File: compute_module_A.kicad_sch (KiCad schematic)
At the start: 14 parts, among them J12 MagJack, J13 Micro_SD_Card_Det, U1 RT9742GGJ5

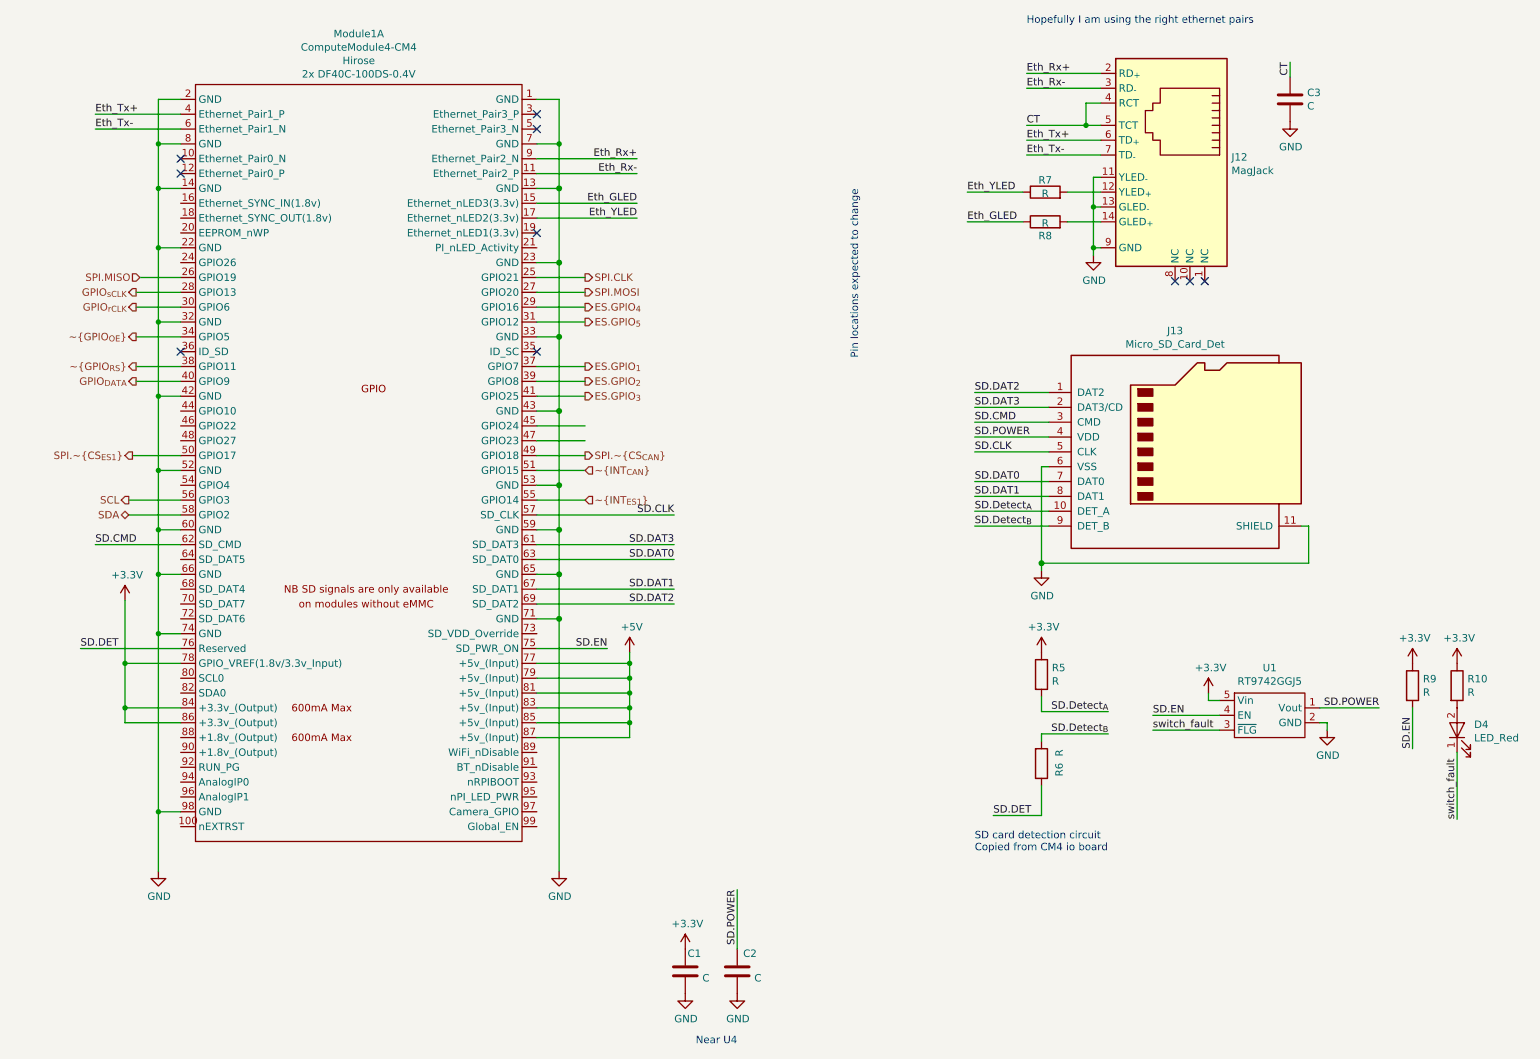
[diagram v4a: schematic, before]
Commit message: Cleaning up
Reassigned reference designators to better match their position on the board.
Moved USB hub IC and related circuits to their own sheet in the schematic.
Tweaked reference designator positions on board to improve visibility.
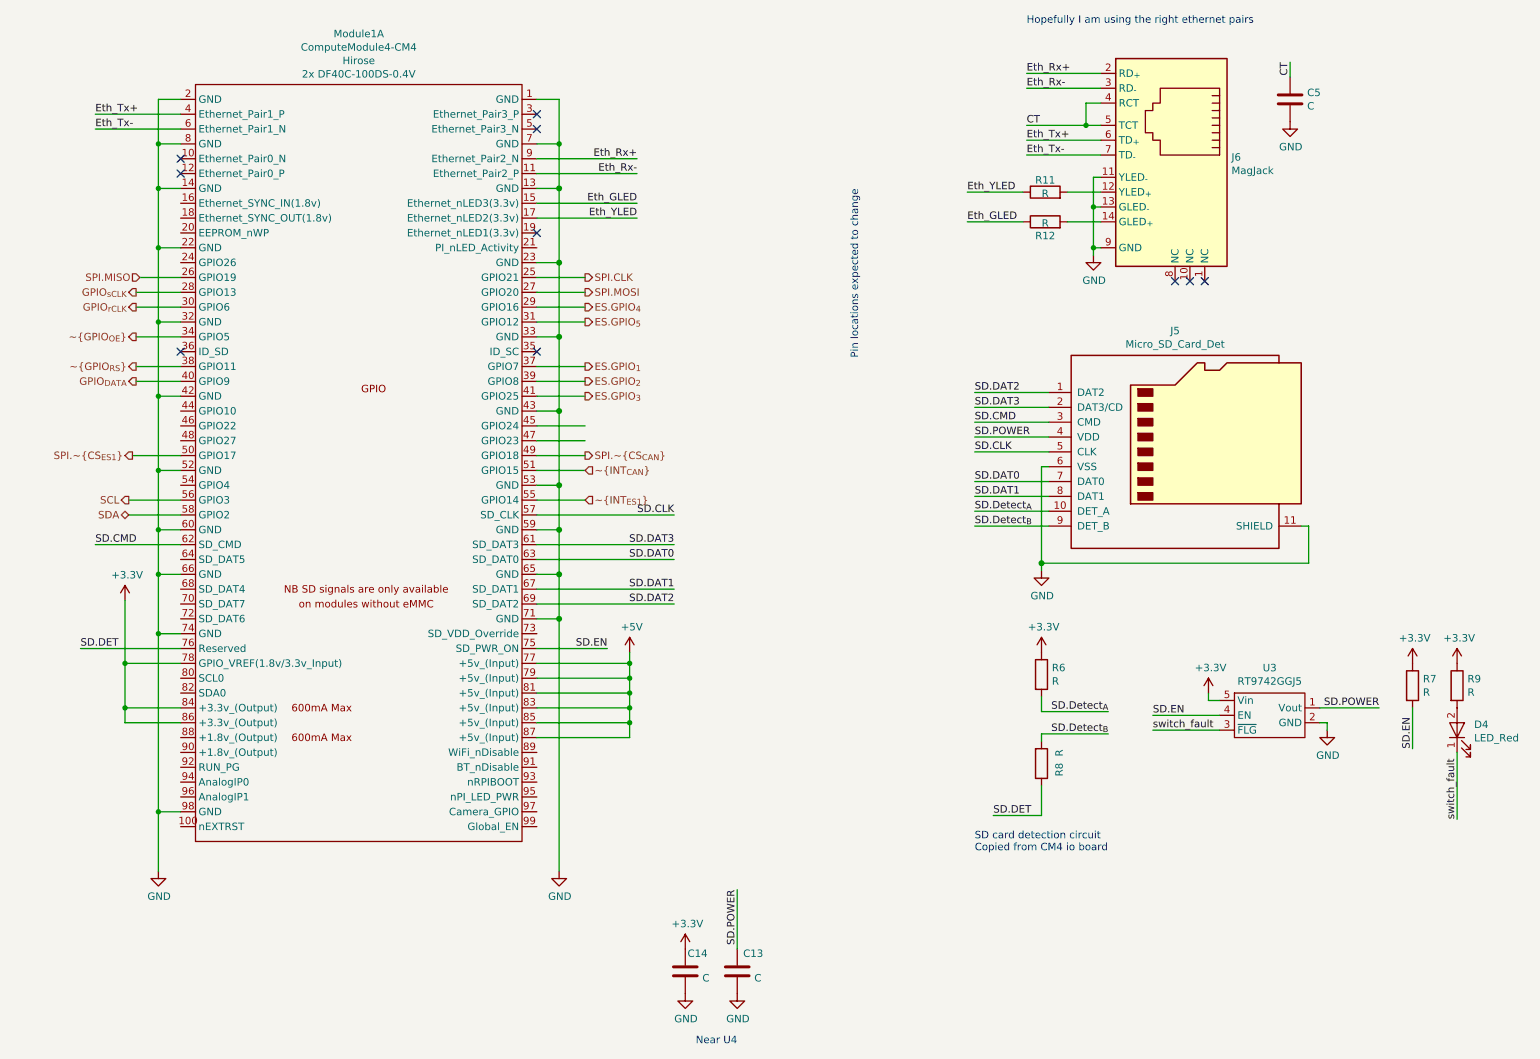
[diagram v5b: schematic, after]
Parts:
- renumbered C2 to C13, C1 to C14, C3 to C5, J13 to J5, J12 to J6, R7 to R11, R8 to R12, R5 to R6, R9 to R7, R6 to R8, R10 to R9, U1 to U3
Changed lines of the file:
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@@
   (title_block
     (title "Dennis")
-    (date "2021-02-26")
-    (rev "0.1.2")
+    (date "2021-03-30")
+    (rev "0.1.3")
     (company "eCafe Racer")
   )
@@
   (junction (at 191.77 53.975) (diameter 0.9144) (color 0 0 0 0))
   (junction (at 191.77 60.96) (diameter 0.9144) (color 0 0 0 0))
+  (no_connect (at 208.28 66.675))
+  (no_connect (at 96.52 78.74))
+  (no_connect (at 96.52 38.1))
+  (no_connect (at 96.52 58.42))
+  (no_connect (at 35.56 45.72))
+  (no_connect (at 35.56 78.74))
   (no_connect (at 35.56 48.26))
-  (no_connect (at 205.74 66.675))
   (no_connect (at 210.82 66.675))
   (no_connect (at 96.52 40.64))
-  (no_connect (at 96.52 58.42))
-  (no_connect (at 96.52 78.74))
-  (no_connect (at 208.28 66.675))
-  (no_connect (at 96.52 38.1))
-  (no_connect (at 35.56 45.72))
-  (no_connect (at 35.56 78.74))
+  (no_connect (at 205.74 66.675))
   (wire (pts (xy 18.415 129.54) (xy 35.56 129.54))
     (stroke (width 0) (type solid) (color 0 0 0 0))
@@
   (symbol (lib_id "Device:R") (at 182.88 133.985 0) (unit 1)
     (in_bom yes) (on_board yes)
-    (property "Reference" "R5" (id 0) (at 184.6581 132.8356 0)
+    (property "Reference" "R6" (id 0) (at 184.6581 132.8356 0)
       (effects (font (size 1.27 1.27)) (justify left))
     )
@@
   (symbol (lib_id "Device:R") (at 182.88 149.225 0) (mirror x) (unit 1)
     (in_bom yes) (on_board yes)
-    (property "Reference" "R6" (id 0) (at 185.9281 149.1044 90)
+    (property "Reference" "R8" (id 0) (at 185.9281 149.1044 90)
       (effects (font (size 1.27 1.27)) (justify left))
     )
@@
   (symbol (lib_id "Device:R") (at 183.515 51.435 90) (unit 1)
     (in_bom yes) (on_board yes)
-    (property "Reference" "R7" (id 0) (at 183.515 49.3838 90))
+    (property "Reference" "R11" (id 0) (at 183.515 49.3838 90))
     (property "Value" "R" (id 1) (at 183.515 51.6825 90))
     (property "Footprint" "Resistor_SMD:R_0805_2012Metric" (id 2) (at 183.515 53.213 90)
@@
   (symbol (lib_id "Device:R") (at 183.515 56.515 90) (unit 1)
     (in_bom yes) (on_board yes)
-    (property "Reference" "R8" (id 0) (at 183.515 58.9088 90))
+    (property "Reference" "R12" (id 0) (at 183.515 58.9088 90))
     (property "Value" "R" (id 1) (at 183.515 56.7625 90))
     (property "Footprint" "Resistor_SMD:R_0805_2012Metric" (id 2) (at 183.515 58.293 90)
@@
   (symbol (lib_id "Device:R") (at 246.38 135.89 0) (unit 1)
     (in_bom yes) (on_board yes)
-    (property "Reference" "R9" (id 0) (at 248.1581 134.7406 0)
+    (property "Reference" "R7" (id 0) (at 248.1581 134.7406 0)
       (effects (font (size 1.27 1.27)) (justify left))
     )
@@
   (symbol (lib_id "Device:R") (at 254 135.89 0) (unit 1)
     (in_bom yes) (on_board yes)
-    (property "Reference" "R10" (id 0) (at 255.7781 134.7406 0)
+    (property "Reference" "R9" (id 0) (at 255.7781 134.7406 0)
       (effects (font (size 1.27 1.27)) (justify left))
     )
@@
   (symbol (lib_id "Device:C") (at 121.92 184.785 0) (unit 1)
     (in_bom yes) (on_board yes)
-    (property "Reference" "C1" (id 0) (at 122.3011 181.7306 0)
+    (property "Reference" "C14" (id 0) (at 122.3011 181.7306 0)
       (effects (font (size 1.27 1.27)) (justify left))
     )
@@
   (symbol (lib_id "Device:C") (at 130.81 184.785 0) (unit 1)
     (in_bom yes) (on_board yes)
-    (property "Reference" "C2" (id 0) (at 131.8261 181.7306 0)
+    (property "Reference" "C13" (id 0) (at 131.8261 181.7306 0)
       (effects (font (size 1.27 1.27)) (justify left))
     )
@@
   (symbol (lib_id "Device:C") (at 225.425 35.56 0) (unit 1)
     (in_bom yes) (on_board yes)
-    (property "Reference" "C3" (id 0) (at 228.3461 34.4106 0)
+    (property "Reference" "C5" (id 0) (at 228.3461 34.4106 0)
       (effects (font (size 1.27 1.27)) (justify left))
     )
@@
   (symbol (lib_id "symbols:RT9742GGJ5") (at 221.615 140.97 0) (unit 1)
     (in_bom yes) (on_board yes)
-    (property "Reference" "U1" (id 0) (at 221.9325 132.8482 0))
+    (property "Reference" "U3" (id 0) (at 221.9325 132.8482 0))
     (property "Value" "RT9742GGJ5" (id 1) (at 221.9325 135.1469 0))
     (property "Footprint" "Package_TO_SOT_SMD:SOT-23-5" (id 2) (at 221.615 138.43 0)
@@
   (symbol (lib_id "symbols:MagJack") (at 199.39 41.275 0) (unit 1)
     (in_bom yes) (on_board yes)
-    (property "Reference" "J12" (id 0) (at 215.3921 45.4533 0)
+    (property "Reference" "J6" (id 0) (at 215.3921 45.4533 0)
       (effects (font (size 1.27 1.27)) (justify left))
     )
@@
   (symbol (lib_id "symbols:Micro_SD_Card_Det") (at 207.01 95.885 0) (unit 1)
     (in_bom yes) (on_board yes)
-    (property "Reference" "J13" (id 0) (at 205.74 75.1648 0))
+    (property "Reference" "J5" (id 0) (at 205.74 75.1648 0))
     (property "Value" "Micro_SD_Card_Det" (id 1) (at 205.74 77.4635 0))
     (property "Footprint" "Connector_Card:microSD_HC_Hirose_DM3D-SF" (id 2) (at 259.08 78.105 0)

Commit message: migrated computers
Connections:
- net SPI.~CS_{CAN} renamed SPI.~{CS_{CAN}}
- net SPI.~CS_{ES1} renamed SPI.~{CS_{ES1}}
- net ~GPIO_{OE} renamed ~{GPIO_{OE}}
- net ~GPIO_{RS} renamed ~{GPIO_{RS}}
- net ~INT_{CAN} renamed ~{INT_{CAN}}
- net ~INT_{ES1} renamed ~{INT_{ES1}}
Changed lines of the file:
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@@
-(kicad_sch (version 20201015) (generator eeschema)
+(kicad_sch (version 20210621) (generator eeschema)
   (paper "A")
   (title_block
@@
   (junction (at 191.77 53.975) (diameter 0.9144) (color 0 0 0 0))
   (junction (at 191.77 60.96) (diameter 0.9144) (color 0 0 0 0))
+  (no_connect (at 35.56 45.72))
+  (no_connect (at 35.56 48.26))
+  (no_connect (at 35.56 78.74))
+  (no_connect (at 96.52 38.1))
+  (no_connect (at 96.52 40.64))
+  (no_connect (at 96.52 58.42))
+  (no_connect (at 96.52 78.74))
+  (no_connect (at 205.74 66.675))
   (no_connect (at 208.28 66.675))
-  (no_connect (at 96.52 78.74))
-  (no_connect (at 96.52 38.1))
-  (no_connect (at 96.52 58.42))
-  (no_connect (at 35.56 45.72))
-  (no_connect (at 35.56 78.74))
-  (no_connect (at 35.56 48.26))
   (no_connect (at 210.82 66.675))
-  (no_connect (at 96.52 40.64))
-  (no_connect (at 205.74 66.675))
   (wire (pts (xy 18.415 129.54) (xy 35.56 129.54))
     (stroke (width 0) (type solid) (color 0 0 0 0))
@@
     (effects (font (size 1.27 1.27)) (justify right))
   )
-  (hierarchical_label "SPI.~CS_{ES1}" (shape output) (at 27.305 96.52 180)
+  (hierarchical_label "SPI.~{CS_{ES1}}" (shape output) (at 27.305 96.52 180)
     (effects (font (size 1.27 1.27)) (justify right))
   )
@@
     (effects (font (size 1.27 1.27)) (justify right))
   )
-  (hierarchical_label "~GPIO_{OE}" (shape output) (at 27.94 76.2 180)
+  (hierarchical_label "~{GPIO_{OE}}" (shape output) (at 27.94 76.2 180)
     (effects (font (size 1.27 1.27)) (justify right))
   )
-  (hierarchical_label "~GPIO_{RS}" (shape output) (at 27.94 81.28 180)
+  (hierarchical_label "~{GPIO_{RS}}" (shape output) (at 27.94 81.28 180)
     (effects (font (size 1.27 1.27)) (justify right))
   )
@@
     (effects (font (size 1.27 1.27)) (justify left))
   )
-  (hierarchical_label "SPI.~CS_{CAN}" (shape output) (at 104.775 96.52 0)
+  (hierarchical_label "SPI.~{CS_{CAN}}" (shape output) (at 104.775 96.52 0)
     (effects (font (size 1.27 1.27)) (justify left))
   )
-  (hierarchical_label "~INT_{CAN}" (shape input) (at 104.775 99.06 0)
+  (hierarchical_label "~{INT_{CAN}}" (shape input) (at 104.775 99.06 0)
     (effects (font (size 1.27 1.27)) (justify left))
   )
-  (hierarchical_label "~INT_{ES1}" (shape input) (at 104.775 104.14 0)
+  (hierarchical_label "~{INT_{ES1}}" (shape input) (at 104.775 104.14 0)
     (effects (font (size 1.27 1.27)) (justify left))
   )
@@
       (effects (font (size 1.27 1.27)) hide)
     )
+    (pin "1")
   )
   (symbol (lib_id "power:+5V") (at 112.395 130.175 0) (unit 1)
@@
       (effects (font (size 1.27 1.27)) hide)
     )
+    (pin "1")
   )
   (symbol (lib_id "power:+3.3V") (at 121.92 180.975 0) (unit 1)
@@
       (effects (font (size 1.27 1.27)) hide)
     )
+    (pin "1")
   )
   (symbol (lib_id "power:+3.3V") (at 182.88 130.175 0) (unit 1)
@@
       (effects (font (size 1.27 1.27)) hide)
     )
+    (pin "1")
   )
   (symbol (lib_id "power:+3.3V") (at 211.455 137.16 0) (unit 1)
@@
       (effects (font (size 1.27 1.27)) hide)
     )
+    (pin "1")
   )
   (symbol (lib_id "power:+3.3V") (at 246.38 132.08 0) (unit 1)
@@
       (effects (font (size 1.27 1.27)) hide)
     )
+    (pin "1")
   )
   (symbol (lib_id "power:+3.3V") (at 254 132.08 0) (unit 1)
@@
       (effects (font (size 1.27 1.27)) hide)
     )
+    (pin "1")
   )
   (symbol (lib_id "power:GND") (at 31.75 167.64 0) (unit 1)
@@
       (effects (font (size 1.27 1.27)) hide)
     )
+    (pin "1")
   )
   (symbol (lib_id "power:GND") (at 100.33 167.64 0) (unit 1)
@@
       (effects (font (size 1.27 1.27)) hide)
     )
+    (pin "1")
   )
   (symbol (lib_id "power:GND") (at 121.92 188.595 0) (unit 1)
@@
       (effects (font (size 1.27 1.27)) hide)
     )
+    (pin "1")
   )
   (symbol (lib_id "power:GND") (at 130.81 188.595 0) (unit 1)
@@
       (effects (font (size 1.27 1.27)) hide)
     )
+    (pin "1")
   )
   (symbol (lib_id "power:GND") (at 182.88 116.205 0) (unit 1)
@@
       (effects (font (size 1.27 1.27)) hide)
     )
+    (pin "1")
   )
   (symbol (lib_id "power:GND") (at 191.77 62.23 0) (unit 1)
@@
       (effects (font (size 1.27 1.27)) hide)
     )
+    (pin "1")
   )
   (symbol (lib_id "power:GND") (at 225.425 39.37 0) (unit 1)
@@
       (effects (font (size 1.27 1.27)) hide)
     )
+    (pin "1")
   )
   (symbol (lib_id "power:GND") (at 231.775 143.51 0) (unit 1)
@@
       (effects (font (size 1.27 1.27)) hide)
     )
+    (pin "1")
   )
   (symbol (lib_id "Device:R") (at 182.88 133.985 0) (unit 1)
@@
       (effects (font (size 1.27 1.27)) hide)
     )
+    (pin "1")
+    (pin "2")
   )
   (symbol (lib_id "Device:R") (at 182.88 149.225 0) (mirror x) (unit 1)
@@
       (effects (font (size 1.27 1.27)) hide)
     )
+    (pin "1")
+    (pin "2")
   )
   (symbol (lib_id "Device:R") (at 183.515 51.435 90) (unit 1)
@@
       (effects (font (size 1.27 1.27)) hide)
     )
+    (pin "1")
+    (pin "2")
   )
   (symbol (lib_id "Device:R") (at 183.515 56.515 90) (unit 1)
@@
       (effects (font (size 1.27 1.27)) hide)
     )
+    (pin "1")
+    (pin "2")
   )
   (symbol (lib_id "Device:R") (at 246.38 135.89 0) (unit 1)
@@
       (effects (font (size 1.27 1.27)) hide)
     )
+    (pin "1")
+    (pin "2")
   )
   (symbol (lib_id "Device:R") (at 254 135.89 0) (unit 1)
@@
       (effects (font (size 1.27 1.27)) hide)
     )
+    (pin "1")
+    (pin "2")
   )
   (symbol (lib_id "Custom-Symbols:LED_Red") (at 254 143.51 90) (unit 1)
@@
       (effects (font (size 1.27 1.27)) hide)
     )
+    (pin "1")
+    (pin "2")
   )
   (symbol (lib_id "Device:C") (at 121.92 184.785 0) (unit 1)
@@
       (effects (font (size 1.27 1.27)) hide)
     )
+    (pin "1")
+    (pin "2")
   )
   (symbol (lib_id "Device:C") (at 130.81 184.785 0) (unit 1)
@@
       (effects (font (size 1.27 1.27)) hide)
     )
+    (pin "1")
+    (pin "2")
   )
   (symbol (lib_id "Device:C") (at 225.425 35.56 0) (unit 1)
@@
       (effects (font (size 1.27 1.27)) hide)
     )
+    (pin "1")
+    (pin "2")
   )
   (symbol (lib_id "symbols:RT9742GGJ5") (at 221.615 140.97 0) (unit 1)
@@
       (effects (font (size 1.27 1.27)) hide)
     )
+    (pin "1")
+    (pin "2")
+    (pin "3")
+    (pin "4")
+    (pin "5")
   )
   (symbol (lib_id "symbols:MagJack") (at 199.39 41.275 0) (unit 1)
@@
       (effects (font (size 1.27 1.27)) hide)
     )
+    (pin "1")
+    (pin "10")
+    (pin "11")
+    (pin "12")
+    (pin "13")
+    (pin "14")
+    (pin "2")
+    (pin "3")
+    (pin "4")
+    (pin "5")
+    (pin "6")
+    (pin "7")
+    (pin "8")
+    (pin "9")
   )
   (symbol (lib_id "symbols:Micro_SD_Card_Det") (at 207.01 95.885 0) (unit 1)
@@
       (effects (font (size 1.27 1.27)) hide)
     )
+    (pin "1")
+    (pin "10")
+    (pin "11")
+    (pin "2")
+    (pin "3")
+    (pin "4")
+    (pin "5")
+    (pin "6")
+    (pin "7")
+    (pin "8")
+    (pin "9")
   )
   (symbol (lib_id "symbols:ComputeModule4-CM4") (at 68.58 91.44 0) (unit 1)
@@
     (property "Field4" "Hirose" (id 4) (at 66.04 28.9368 0))
     (property "Field5" "2x DF40C-100DS-0.4V" (id 5) (at 66.04 31.2355 0))
+    (pin "1")
+    (pin "10")
+    (pin "100")
+    (pin "11")
+    (pin "12")
+    (pin "13")
+    (pin "14")
+    (pin "15")
+    (pin "16")
+    (pin "17")
+    (pin "18")
+    (pin "19")
+    (pin "2")
+    (pin "20")
+    (pin "21")
+    (pin "22")
+    (pin "23")
+    (pin "24")
+    (pin "25")
+    (pin "26")
+    (pin "27")
+    (pin "28")
+    (pin "29")
+    (pin "3")
+    (pin "30")
+    (pin "31")
+    (pin "32")
+    (pin "33")
+    (pin "34")
+    (pin "35")
+    (pin "36")
+    (pin "37")
+    (pin "38")
+    (pin "39")
+    (pin "4")
+    (pin "40")
+    (pin "41")
+    (pin "42")
+    (pin "43")
+    (pin "44")
+    (pin "45")
+    (pin "46")
+    (pin "47")
+    (pin "48")
+    (pin "49")
+    (pin "5")
+    (pin "50")
+    (pin "51")
+    (pin "52")
+    (pin "53")
+    (pin "54")
+    (pin "55")
+    (pin "56")
+    (pin "57")
+    (pin "58")
+    (pin "59")
+    (pin "6")
+    (pin "60")
+    (pin "61")
+    (pin "62")
+    (pin "63")
+    (pin "64")
+    (pin "65")
+    (pin "66")
+    (pin "67")
+    (pin "68")
+    (pin "69")
+    (pin "7")
+    (pin "70")
+    (pin "71")
+    (pin "72")
+    (pin "73")
+    (pin "74")
+    (pin "75")
+    (pin "76")
+    (pin "77")
+    (pin "78")
+    (pin "79")
+    (pin "8")
+    (pin "80")
+    (pin "81")
+    (pin "82")
+    (pin "83")
+    (pin "84")
+    (pin "85")
+    (pin "86")
+    (pin "87")
+    (pin "88")
+    (pin "89")
+    (pin "9")
+    (pin "90")
+    (pin "91")
+    (pin "92")
+    (pin "93")
+    (pin "94")
+    (pin "95")
+    (pin "96")
+    (pin "97")
+    (pin "98")
+    (pin "99")
   )
 )
